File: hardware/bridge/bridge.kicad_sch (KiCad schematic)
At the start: 14 parts, among them U1 SIT3088EEUA, U3 SIT3088EEUA

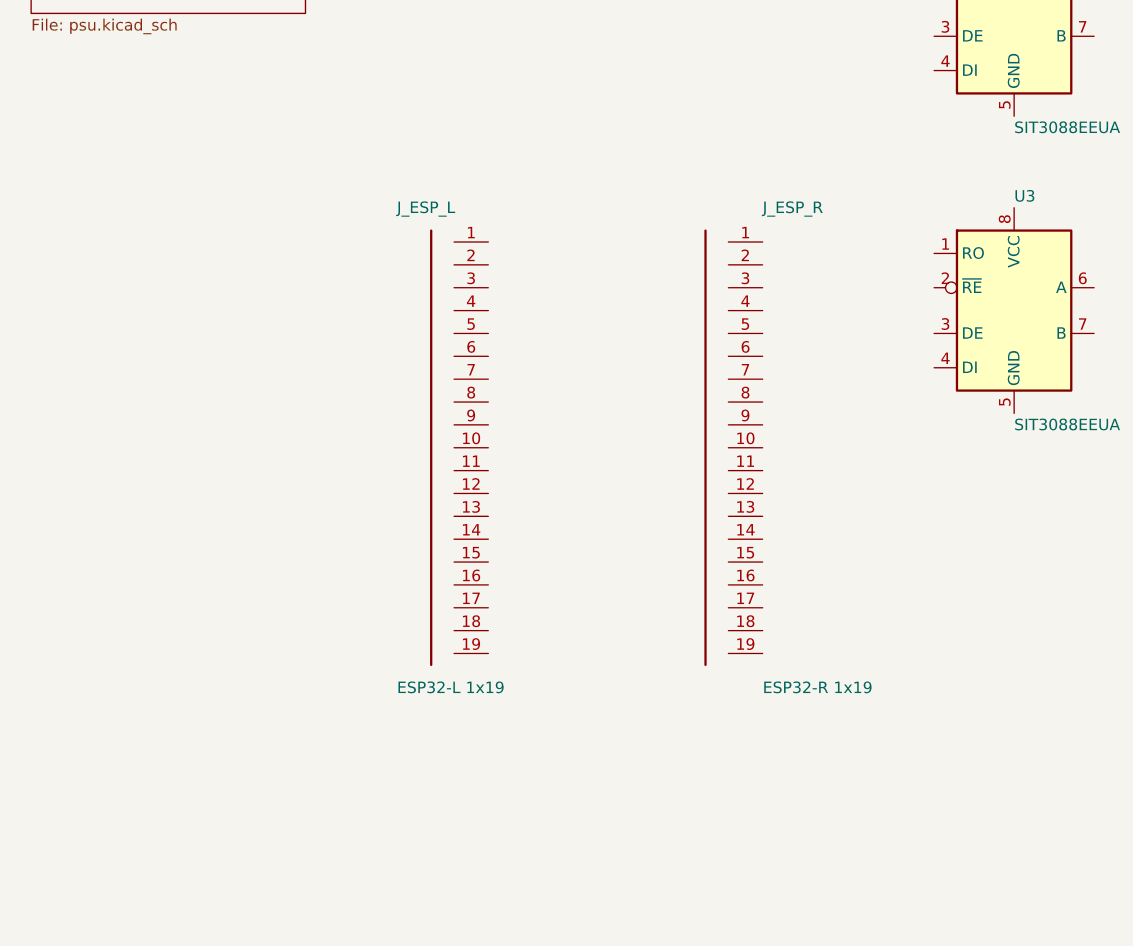
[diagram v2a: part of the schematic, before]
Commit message: hardware: bridge switches to soldered ESP32-S3-MINI-1-N8 + USB-C
Replaces the socketed ESP32-DevKitC-V4 (1x19 headers) with a soldered
ESP32-S3-MINI-1-N8 module driven over native USB 2.0. No USB-UART bridge,
no auto-reset circuit — the S3's native USB handles programming and the
serial console.

Added on the main schematic:
- U4 ESP32-S3-MINI-1-N8 (LCSC C2913206, tsumikoro:ESP32-S3-MINI-1 footprint
  with 3D STEP model)
- J_USB 16-pin USB-C receptacle (LCSC C2927039,
  Connector_USB:USB_C_Receptacle_GCT_USB4085 footprint + 3D model)
- SW_BOOT, SW_RESET tact switches (LCSC C318884, XKB TS-1187A)
- R_CC1, R_CC2: 5.1k 0402 CC pull-downs for USB-C sink-device marking
- R_EN, R_BOOT: 10k 0402 basic pull-ups on EN and GPIO0
- Text annotation with wiring guide

Removed:
- J_ESP_L, J_ESP_R (the two 1x19 female pin sockets)
- Conn_01x19 lib_symbol

Vendored the Espressif library parts in hardware/lib/ (CC-BY-SA 4.0) so
the project stays self-contained — no PCM install dependency:
- hardware/lib/footprints.pretty/ESP32-S3-MINI-1.kicad_mod
- hardware/lib/footprints.pretty/ESP32-S3-DevKitC.kicad_mod
- hardware/lib/3dmodels/ESP32-S3-MINI-1.STEP
- ESP32-S3-MINI-1 and ESP32-S3-DevKitC symbols merged into
  hardware/lib/symbols/tsumikoro.kicad_sym
- hardware/lib/ATTRIBUTIONS.md documenting upstream source + license

The DevKitC variant footprint is vendored alongside but not placed on
the current schematic — kept for future board revisions that socket the
full dev kit.

Wiring (nets) still pending — symbols are placed with correct footprints
and 3D models; user draws the connections in KiCad.
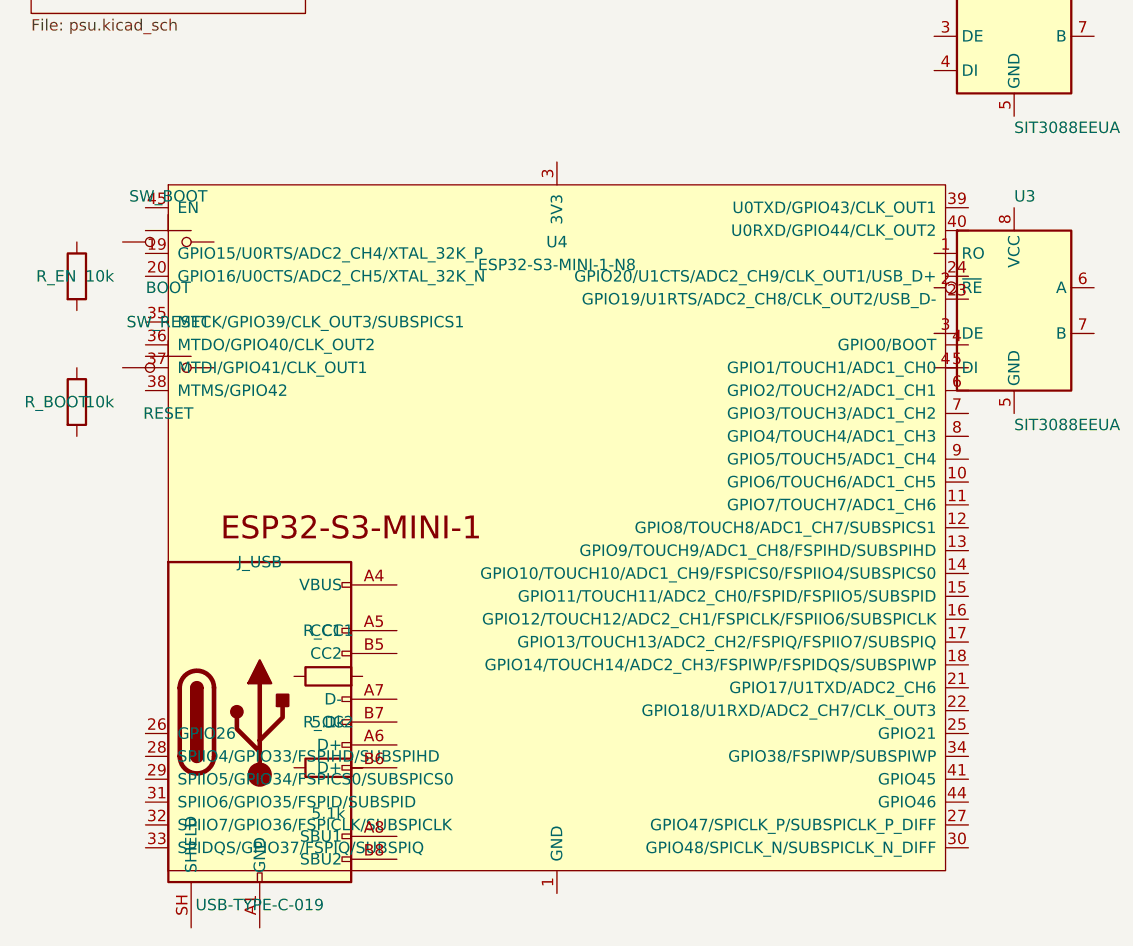
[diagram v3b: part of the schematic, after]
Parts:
- removed J_ESP_L: ESP32-L 1x19, Connector_PinHeader_2.54mm:PinSocket_1x19_P2.54mm_Vertical, symbol Connector_Generic:Conn_01x19
- removed J_ESP_R: ESP32-R 1x19, Connector_PinHeader_2.54mm:PinSocket_1x19_P2.54mm_Vertical, symbol Connector_Generic:Conn_01x19
- added J_USB: USB-TYPE-C-019, Connector_USB:USB_C_Receptacle_GCT_USB4085, symbol Connector:USB_C_Receptacle_USB2.0_16P
- added R_BOOT, R_EN: 10k, Resistor_SMD:R_0402_1005Metric, symbol Device:R
- added R_CC1, R_CC2: 5.1k, Resistor_SMD:R_0402_1005Metric, symbol Device:R
- added SW_BOOT: BOOT, Button_Switch_SMD:SW_Push_1P1T_XKB_TS-1187A, symbol Switch:SW_Push
- added SW_RESET: RESET, Button_Switch_SMD:SW_Push_1P1T_XKB_TS-1187A, symbol Switch:SW_Push
- added U4: ESP32-S3-MINI-1-N8, tsumikoro:ESP32-S3-MINI-1, symbol tsumikoro:ESP32-S3-MINI-1
- JDC1, JDC2: footprint Connector_BarrelJack:BarrelJack_CUI_PJ-063AH_Horizontal -> Connector_BarrelJack:BarrelJack_GCT_DCJ200-10-A_Horizontal
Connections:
- new net: J_USB.A1 (GND), J_USB.A12 (GND), J_USB.B1 (GND), J_USB.B12 (GND)
- new net: J_USB.A4 (VBUS), J_USB.A9 (VBUS), J_USB.B4 (VBUS), J_USB.B9 (VBUS)
- new net: U4.1 (GND), U4.2 (GND), U4.42 (GND), U4.43 (GND), U4.46 (GND), U4.47 (GND), U4.48 (GND), U4.49 (GND), U4.50 (GND), U4.51 (GND), U4.52 (GND), U4.53 (GND), U4.54 (GND), U4.55 (GND), U4.56 (GND), U4.57 (GND), U4.58 (GND), U4.59 (GND), U4.60 (GND), U4.61 (GND), U4.62 (GND), U4.63 (GND), U4.64 (GND), U4.65 (GND)

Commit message: hardware: vendor TS-1187A tact switch footprint + approximate 3D model
KiCad's stock Button_Switch_SMD:SW_Push_1P1T_XKB_TS-1187A footprint
references a STEP file that is missing from the KiCad asset tree — the
button renders as bare pads with no body.

Vendor the footprint as tsumikoro:SW_Push_1P1T_XKB_TS-1187A and repoint
the 3D model at a copy of the CK KMR2 STEP (close-enough tact switch
body, 4.2x3.2 mm vs TS-1187A's 4.5x4.5 mm). Gets us a visible body in
the 3D viewer for layout checks. Replace with a real TS-1187A STEP if
dimensional accuracy matters.

SW_BOOT and SW_RESET on the bridge now use the vendored footprint.
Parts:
- SW_BOOT, SW_RESET: footprint Button_Switch_SMD:SW_Push_1P1T_XKB_TS-1187A -> tsumikoro:SW_Push_1P1T_XKB_TS-1187A
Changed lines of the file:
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@@
 		(property "Reference" "SW_BOOT" (at 40.64 111.76 0) (effects (font (size 1.27 1.27))))
 		(property "Value" "BOOT" (at 40.64 121.92 0) (effects (font (size 1.27 1.27))))
-		(property "Footprint" "Button_Switch_SMD:SW_Push_1P1T_XKB_TS-1187A" (at 40.64 116.84 0) (effects (font (size 1.27 1.27)) hide))
+		(property "Footprint" "tsumikoro:SW_Push_1P1T_XKB_TS-1187A" (at 40.64 116.84 0) (effects (font (size 1.27 1.27)) hide))
 		(property "Datasheet" "~" (at 40.64 116.84 0) (effects (font (size 1.27 1.27)) hide))
 		(property "Description" "Boot-mode button: press while reset to enter download mode (GPIO0)" (at 40.64 116.84 0) (effects (font (size 1.27 1.27)) hide))
@@
 		(property "Reference" "SW_RESET" (at 40.64 125.73 0) (effects (font (size 1.27 1.27))))
 		(property "Value" "RESET" (at 40.64 135.89 0) (effects (font (size 1.27 1.27))))
-		(property "Footprint" "Button_Switch_SMD:SW_Push_1P1T_XKB_TS-1187A" (at 40.64 130.81 0) (effects (font (size 1.27 1.27)) hide))
+		(property "Footprint" "tsumikoro:SW_Push_1P1T_XKB_TS-1187A" (at 40.64 130.81 0) (effects (font (size 1.27 1.27)) hide))
 		(property "Datasheet" "~" (at 40.64 130.81 0) (effects (font (size 1.27 1.27)) hide))
 		(property "Description" "Reset button: pulls EN low" (at 40.64 130.81 0) (effects (font (size 1.27 1.27)) hide))

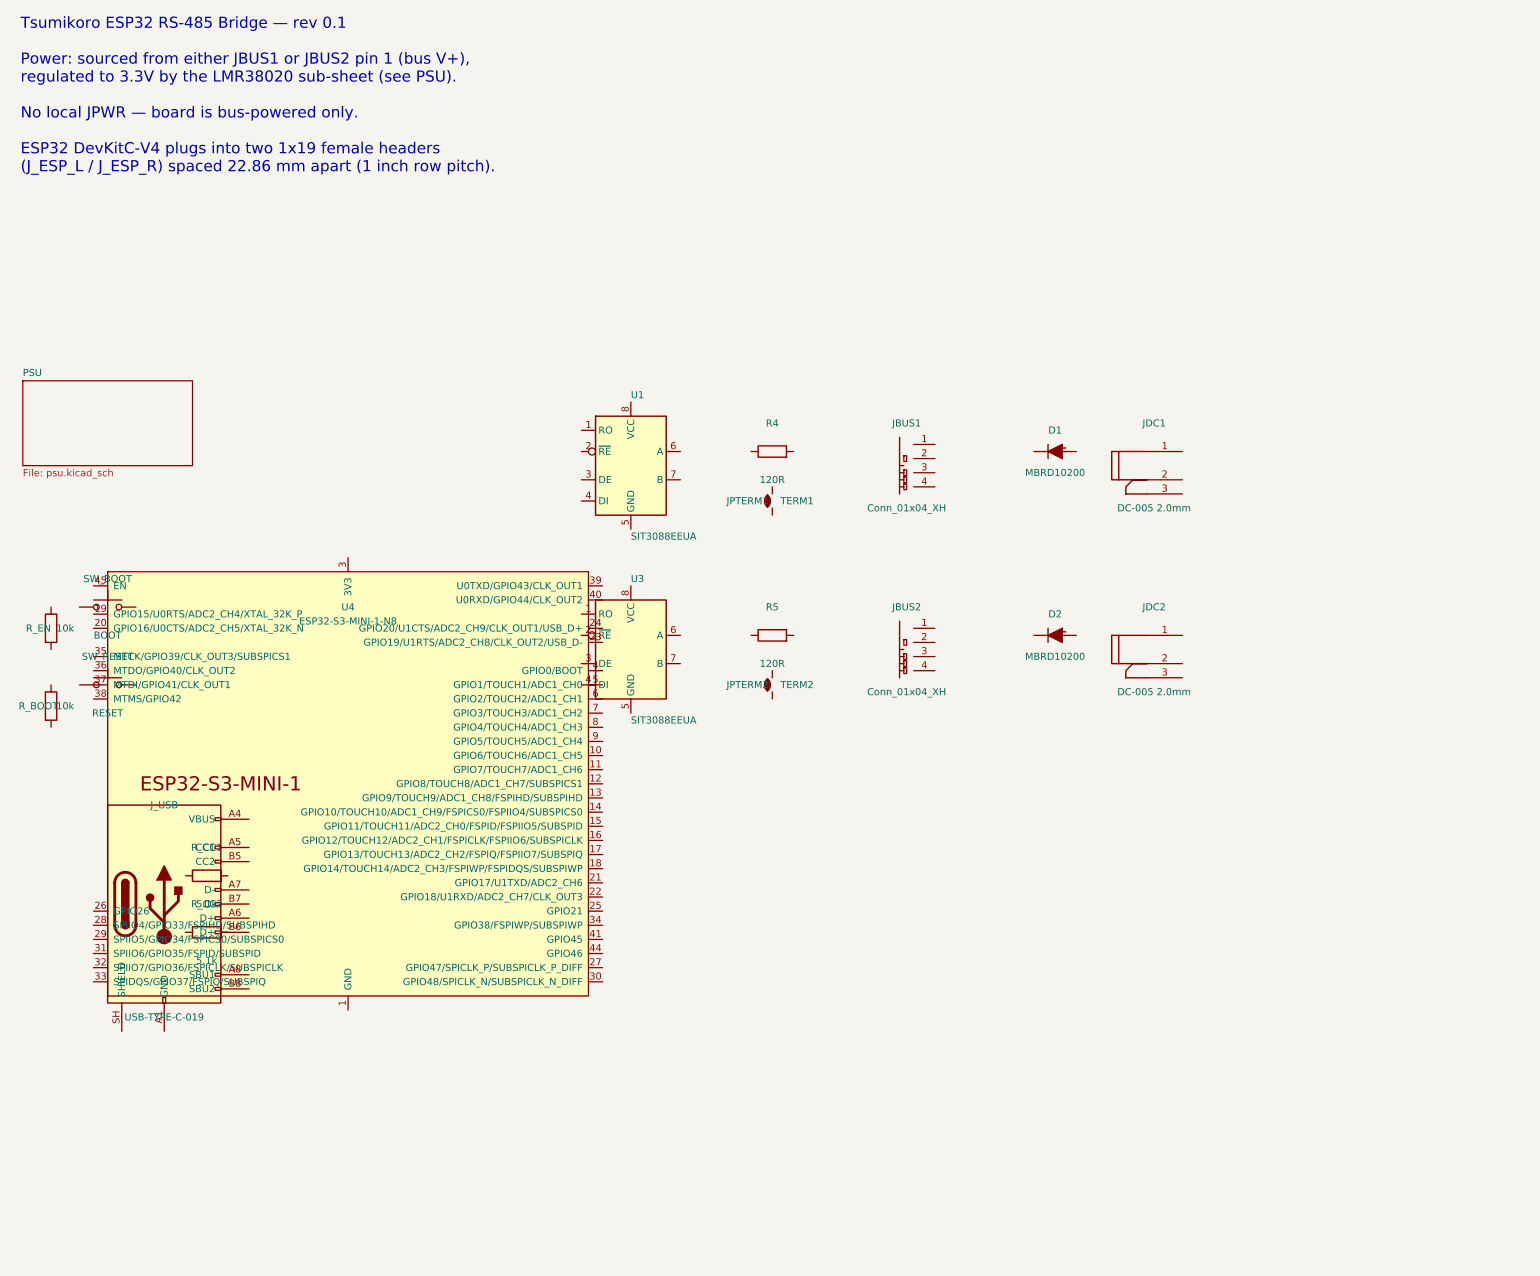
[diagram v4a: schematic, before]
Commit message: hardware: bridge USB-C footprint corrected to SMT 16P with 3D model
Was using Connector_USB:USB_C_Receptacle_GCT_USB4085 — that's the
through-hole mid-mount variant. The USB-TYPE-C-019 (C2927039) is a
top-mount SMT 16-pin USB-C. Switched to
Connector_USB:USB_C_Receptacle_GCT_USB4105-xx-A_16P_TopMnt_Horizontal
which is SMT 16P with the standard pad layout that Chinese clones
(USB-TYPE-C-019, HCTL HC-TYPE-C-16P-01A, Palconn UTC16-G, XKB U262,
etc.) follow, and has a 3D STEP model shipped with KiCad.
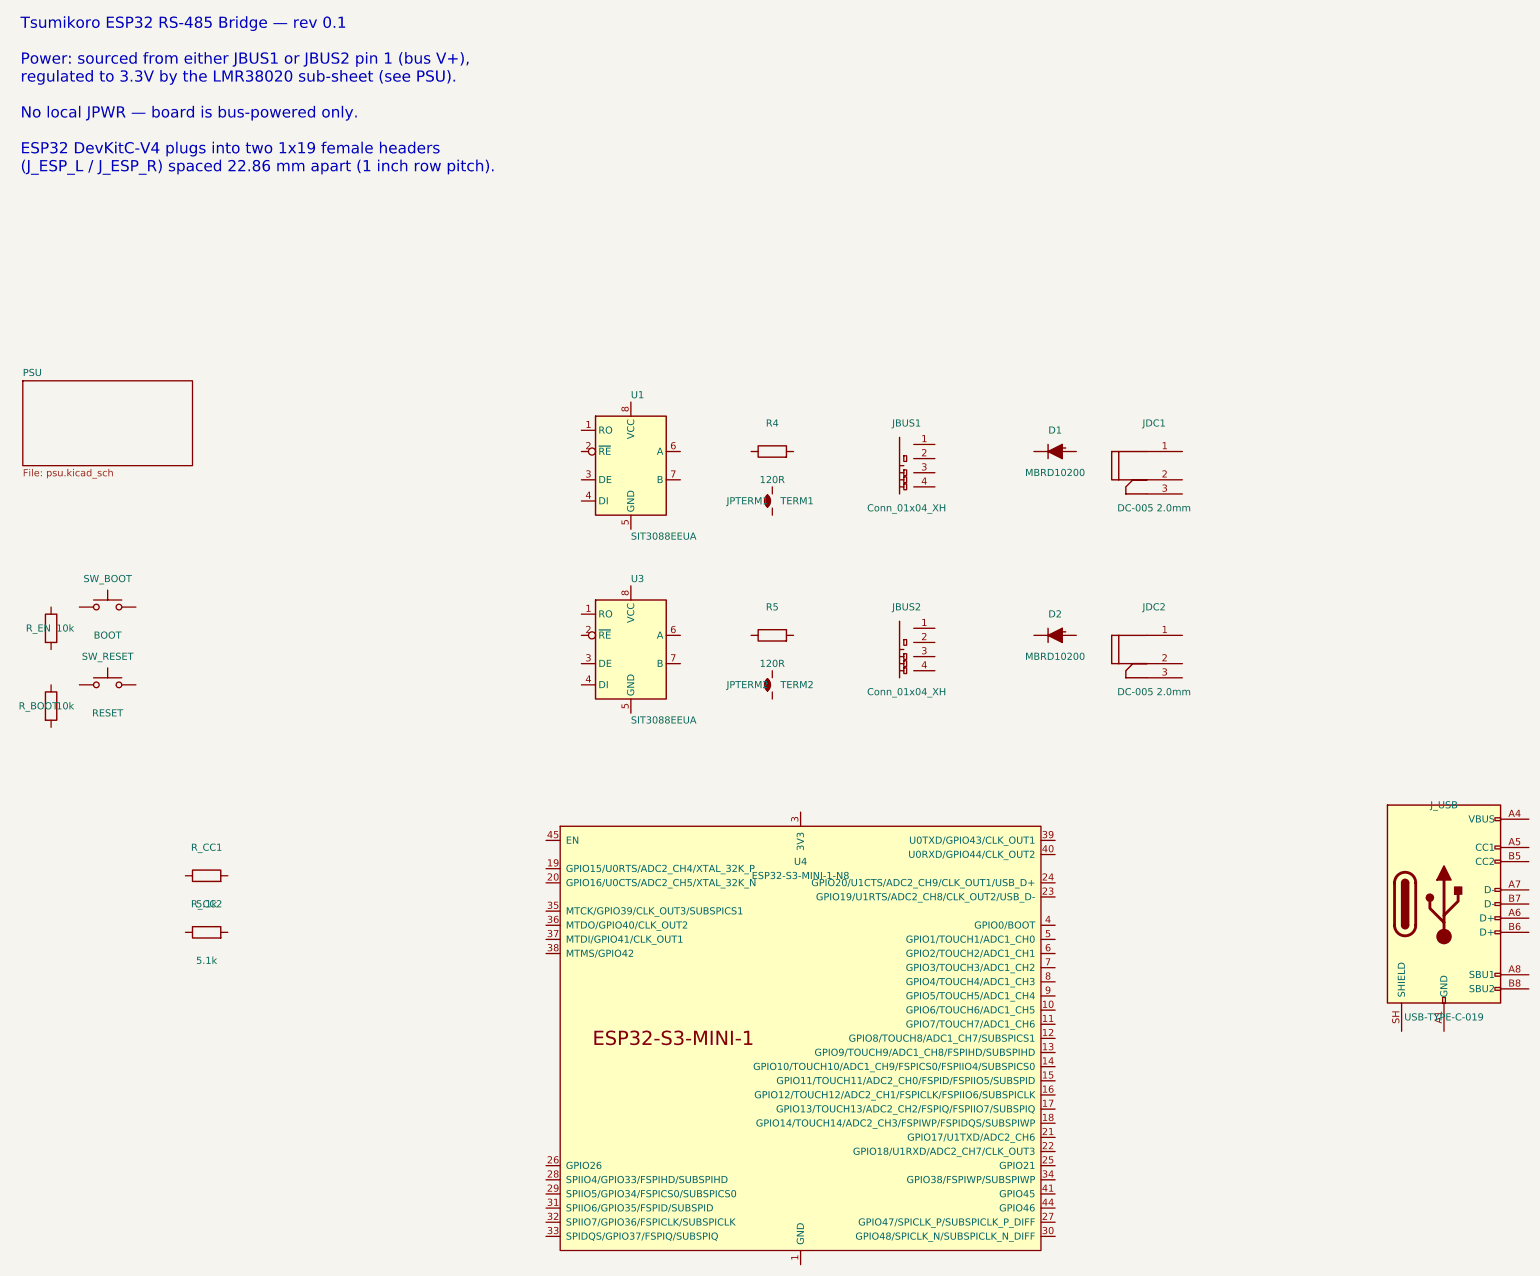
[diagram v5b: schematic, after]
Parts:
- J_USB: footprint Connector_USB:USB_C_Receptacle_GCT_USB4085 -> Connector_USB:USB_C_Receptacle_GCT_USB4105-xx-A_16P_TopMnt_Horizontal

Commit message: ministepper: finalize pin map + sync firmware to hardware rev 0.1
Hardware (schematic + docs) and firmware now share a single source of
truth for the STM32G071G8U6 UFQFPN-28 pinout:

- USART2 on PA2/PA3 (RS-485) — dedicated pins, no SYSCFG remap needed
  (unlike the servo's STM32G030 where PA11/PA12 shared pads with
  PA9/PA10)
- Two independent step timers: TIM1_CH1 on PA8 (STEP1) and TIM2_CH1
  on PA0 (STEP2) — each axis can run at its own rate
- Shared SPI1 (PA5/6/7) to both TMC2130s with software-managed CS on
  PA4 (TMC1) and PA12 (TMC2)
- Shared DRV_ENN on PA11 — pulls both drivers in/out of enable at once
- Per-axis limit switches (PB0, PB3) and DIAG1 stall/fault inputs
  (PB1, PB4)
- I2C1 on PB6/PB7 for expansion
- Status LED on PB5 (moved off PA5 which is now SPI SCK)
- 1 spare GPIO (PB8) for future use

firmware/tsumikoro-ministepper/src/main.c rewritten:
- Switched from USART1 to USART2; DMA request IDs updated
- PIN_* defines added for every pin from the schematic, cross-referenced
  to the hardware doc
- GPIO init configures all driver control lines (CS high, DRV_ENN high
  = off at boot), DIAG inputs, limit inputs with pull-ups, and the DE
  line for RS-485 (starts low = RX)
- Error_Handler moved to LED on PB5
- Bus callback extended to two-axis selector (byte 0 of move/stop
  payload picks axis 1 or 2); GET_STATUS reports both positions
- SPI1 / TIM1 / TIM2 stepper peripheral init still TODO — the real
  step generator will come with the SPI driver + per-axis motion
  planner

Hardware docs:
- CLAUDE.md adds "Ministepper PCB Pin Map" section (authoritative)
- hardware/ministepper/docs/README.md pin map updated to the final
  layout with independent STEP timers; sense-resistor variants
  (0.1 ohm standard vs 0.68 ohm micro / 28BYJ-48) documented
- hardware/TODO.md marks pin map + firmware sync done

Firmware builds clean (23 KB flash, 14.7 KB RAM) on STM32G071G8U6.
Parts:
- renumbered J_USB to J_USB2, R_BOOT to R_BOOT2, R_EN to R_EN2, SW_BOOT to SW_BOOT2, SW_RESET to SW_RESET2
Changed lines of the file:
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@@
 		(in_pos_files yes)
 		(dnp no)
-		(property "Reference" "SW_RESET"
+		(property "Reference" "SW_RESET2"
 			(at 40.64 125.73 0)
 			(show_name no)
@@
 			(project "bridge"
 				(path "/c1d2e3f4-a5b6-7890-1234-567890abcdef"
-					(reference "SW_RESET")
+					(reference "SW_RESET2")
 					(unit 1)
 				)
@@
 		(in_pos_files yes)
 		(dnp no)
-		(property "Reference" "J_USB"
+		(property "Reference" "J_USB2"
 			(at 280.67 152.4 0)
 			(show_name no)
@@
 			(project "bridge"
 				(path "/c1d2e3f4-a5b6-7890-1234-567890abcdef"
-					(reference "J_USB")
+					(reference "J_USB2")
 					(unit 1)
 				)
@@
 		(in_pos_files yes)
 		(dnp no)
-		(property "Reference" "R_BOOT"
+		(property "Reference" "R_BOOT2"
 			(at 28.194 134.62 0)
 			(show_name no)
@@
 			(project "bridge"
 				(path "/c1d2e3f4-a5b6-7890-1234-567890abcdef"
-					(reference "R_BOOT")
+					(reference "R_BOOT2")
 					(unit 1)
 				)
@@
 		(in_pos_files yes)
 		(dnp no)
-		(property "Reference" "R_EN"
+		(property "Reference" "R_EN2"
 			(at 28.194 120.65 0)
 			(show_name no)
@@
 			(project "bridge"
 				(path "/c1d2e3f4-a5b6-7890-1234-567890abcdef"
-					(reference "R_EN")
+					(reference "R_EN2")
 					(unit 1)
 				)
@@
 		(in_pos_files yes)
 		(dnp no)
-		(property "Reference" "SW_BOOT"
+		(property "Reference" "SW_BOOT2"
 			(at 40.64 111.76 0)
 			(show_name no)
@@
 			(project "bridge"
 				(path "/c1d2e3f4-a5b6-7890-1234-567890abcdef"
-					(reference "SW_BOOT")
+					(reference "SW_BOOT2")
 					(unit 1)
 				)
